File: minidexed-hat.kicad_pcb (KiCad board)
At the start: 2 copper layers, 65 x 56 mm, 5 parts, among them J1 RPi_GPIO

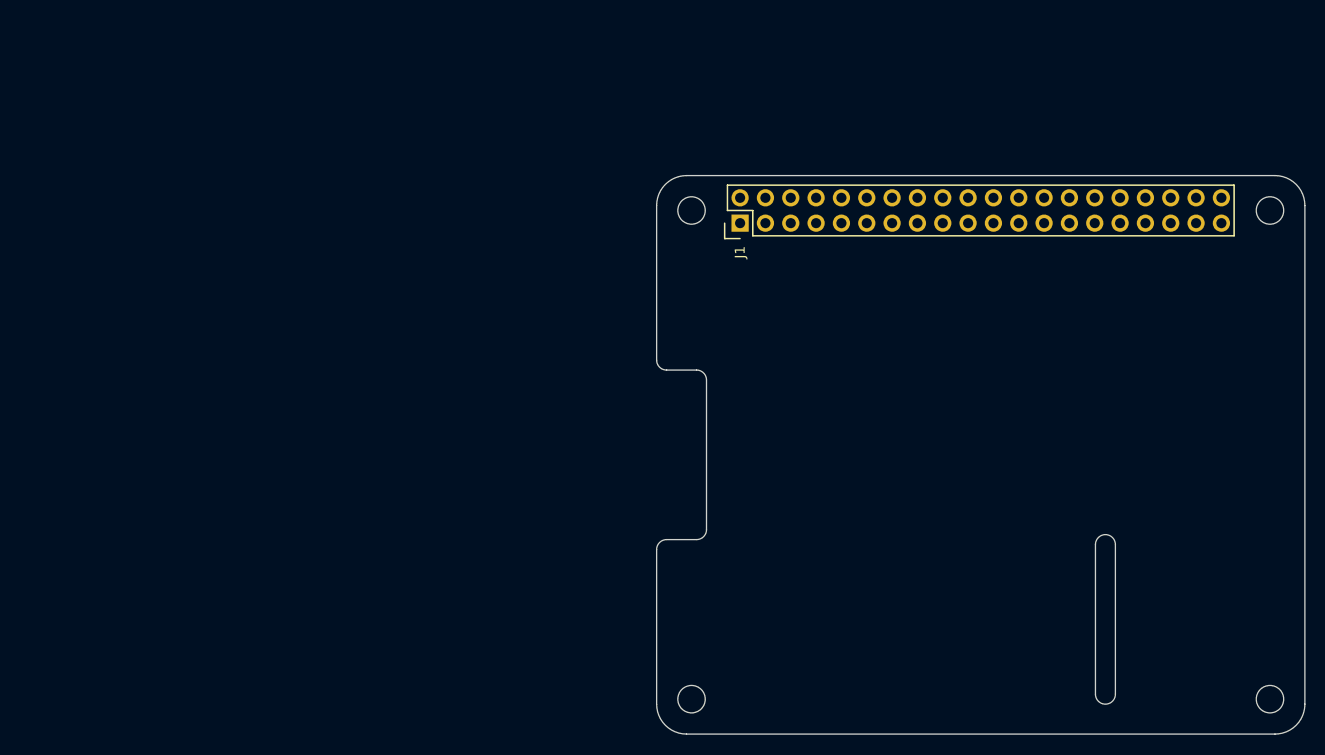
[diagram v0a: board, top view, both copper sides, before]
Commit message: Complete with MIDI and connectors off-board
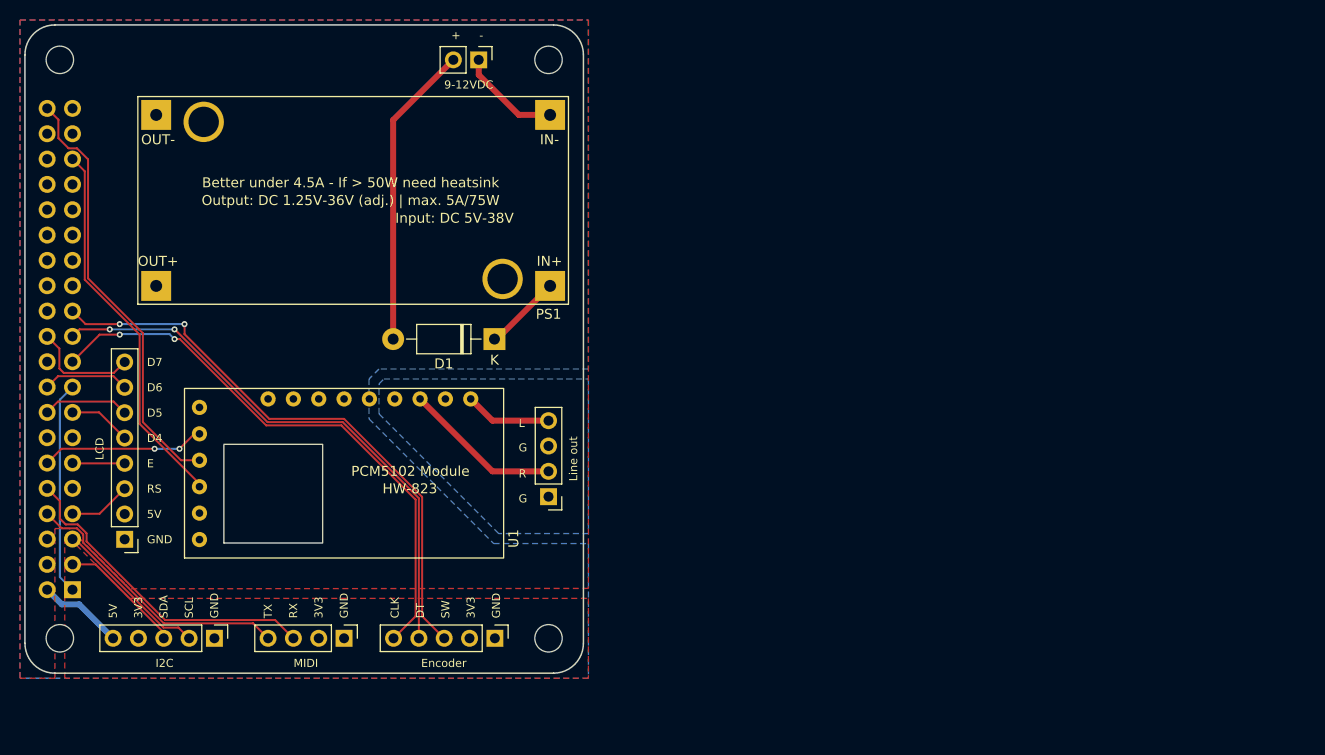
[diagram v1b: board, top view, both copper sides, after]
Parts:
- added D1: 1N4002, Diode_THT:D_DO-41_SOD81_P10.16mm_Horizontal, F.Cu at (97.1, 81.5)
- added J1: MIDI, Connector_PinHeader_2.54mm:PinHeader_1x04_P2.54mm_Vertical, F.Cu at (82.0, 111.5)
- added J2: Line out, Connector_PinHeader_2.54mm:PinHeader_1x04_P2.54mm_Vertical, F.Cu at (102.5, 97.3)
- added J4: Encoder, Connector_PinHeader_2.54mm:PinHeader_1x05_P2.54mm_Vertical, F.Cu at (97.1, 111.5)
- added J5: 9-12V, Connector_PinHeader_2.54mm:PinHeader_1x02_P2.54mm_Vertical, F.Cu at (95.5, 53.5)
- added J6: LCD, Connector_PinHeader_2.54mm:PinHeader_1x08_P2.54mm_Vertical, F.Cu at (60.0, 101.6)
- added J7: I2C, Connector_PinHeader_2.54mm:PinHeader_1x05_P2.54mm_Vertical, F.Cu at (69.0, 111.5)
- added PS1: XL4005_DC-DC, Personal:XL4005_DC-DC, F.Cu at (104.5, 57.2)
- added U1: PCM5102_Module, Personal:PCM5102_HW-823, F.Cu at (66.0, 103.5)
- J3: renamed from J1; footprint RPi_Hat:Pin_Header_Straight_2x20 -> Connector_PinSocket_2.54mm:PinSocket_2x20_P2.54mm_Vertical; moved to B.Cu
- moved H1 122.3 mm to (53.5, 53.5), turned to 90 degrees
- moved J3 98.7 mm to (54.8, 106.6), turned to 0 degrees
- moved H2 96.7 mm to (102.5, 53.5), turned to 90 degrees
- moved H3 76.5 mm to (53.5, 111.5), turned to 90 degrees
- moved H4 15.6 mm to (102.5, 111.5), turned to 90 degrees
- renumbered H2 to H1, H4 to H2, H1 to H3, H3 to H4
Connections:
- J3 pad 1: unconnected-(J1-Pad1) -> +3.3V
- J3 pad 10: unconnected-(J1-Pad10) -> /MIDI_RX
- J3 pad 11: unconnected-(J1-Pad11) -> /LCD_E
- J3 pad 12: unconnected-(J1-Pad12) -> /I2S_BCK
- J3 pad 14: unconnected-(J1-Pad14) -> GND
- J3 pad 15: unconnected-(J1-Pad15) -> /LCD_D4
- J3 pad 16: unconnected-(J1-Pad16) -> /LCD_D5
- J3 pad 17: unconnected-(J1-Pad17) -> +3.3V
- J3 pad 18: unconnected-(J1-Pad18) -> /LCD_D6
- J3 pad 19: unconnected-(J1-Pad19) -> /ENC_CLK
- J3 pad 2: unconnected-(J1-Pad2) -> +5V
- J3 pad 20: unconnected-(J1-Pad20) -> GND
- J3 pad 21: unconnected-(J1-Pad21) -> /ENC_DT
- J3 pad 22: unconnected-(J1-Pad22) -> /LCD_D7
- J3 pad 23: unconnected-(J1-Pad23) -> /ENC_SW
- J3 pad 25: unconnected-(J1-Pad25) -> GND
- J3 pad 3: unconnected-(J1-Pad3) -> /SDA
- J3 pad 30: unconnected-(J1-Pad30) -> GND
- J3 pad 34: unconnected-(J1-Pad34) -> GND
- J3 pad 35: unconnected-(J1-Pad35) -> /I2S_LCK
- J3 pad 39: unconnected-(J1-Pad39) -> GND
- J3 pad 4: unconnected-(J1-Pad4) -> +5V
- J3 pad 40: unconnected-(J1-Pad40) -> /I2S_DIN
- J3 pad 5: unconnected-(J1-Pad5) -> /SCL
- J3 pad 6: unconnected-(J1-Pad6) -> GND
- J3 pad 7: unconnected-(J1-Pad7) -> /LCD_RS
- J3 pad 8: unconnected-(J1-Pad8) -> /MIDI_TX
- J3 pad 9: unconnected-(J1-Pad9) -> GND
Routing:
- net /ENC_SW: track 0.00 -> 58.5 mm, vias 0 -> 2
- net /ENC_CLK: track 0.00 -> 57.2 mm, vias 0 -> 2
- net /ENC_DT: track 0.00 -> 56.1 mm, vias 0 -> 2
- net /I2S_DIN: track 0.00 -> 43.2 mm
- net /I2S_LCK: track 0.00 -> 38.1 mm
- net /MIDI_RX: track 0.00 -> 32.4 mm
- net /+VIN: track 0.00 -> 30.5 mm
- net /MIDI_TX: track 0.00 -> 27.8 mm
- net +3.3V: track 0.00 -> 21.4 mm
- net /I2S_BCK: track 0.00 -> 16.5 mm, vias 0 -> 2
- net /OUT_R: track 0.00 -> 15.9 mm
- net /SCL: track 0.00 -> 15.8 mm
- net /SDA: track 0.00 -> 12.6 mm
- net /LCD_D7: track 0.00 -> 10.9 mm
- net /-VIN: track 0.00 -> 10.3 mm
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- added copper zone on F.Cu, net +3.3V
- added copper zone on F.Cu, net +5V
- added copper zone on B.Cu, net GND
- added copper zone on B.Cu, net GNDA
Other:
- board size 65 x 56 mm -> 56 x 65 mm
- board text added: "+"
- board text added: "-"
- board text added: "3V3"
- board text added: "5V"
- board text added: "9-12VDC"
- board text added: "CLK"
- board text added: "D4"
- board text added: "D5"
- board text added: "D6"
- board text added: "D7"
- board text added: "DT"
- board text added: "E"
- board text added: "Encoder"
- board text added: "G"
- board text added: "GND"
- board text added: "I2C"
- board text added: "L"
- board text added: "LCD"
- board text added: "Line out"
- board text added: "MIDI"
- board text added: "R"
- board text added: "RS"
- board text added: "RX"
- board text added: "SCL"
- board text added: "SDA"
- board text added: "SW"
- board text added: "TX"
